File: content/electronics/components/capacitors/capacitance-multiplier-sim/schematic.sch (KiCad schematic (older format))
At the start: 7 parts, among them Q1 2N2222

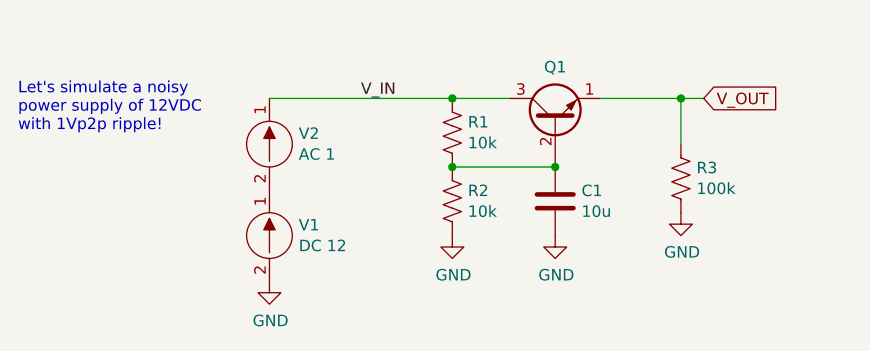
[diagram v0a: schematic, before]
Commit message: Updated the info on capacitance multipliers.
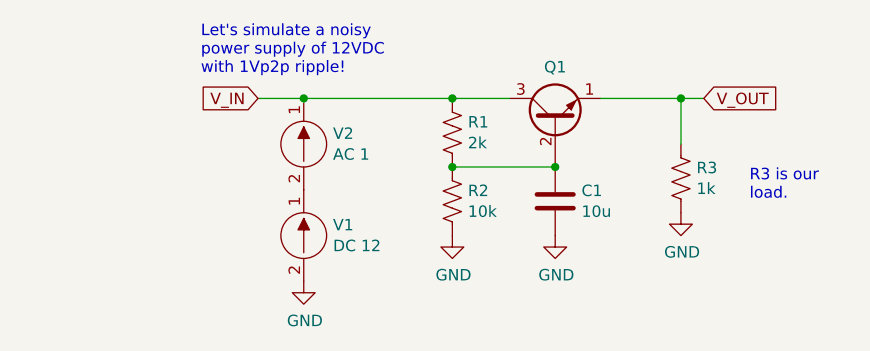
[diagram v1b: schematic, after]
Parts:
- R1: value 10k -> 2k
- R3: value 100k -> 1k
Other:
- note added: "R3 is our\nload."
- moved on the sheet: V1, V2
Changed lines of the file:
@@
 P 4050 3350
 F 0 "R1" H 3982 3304 50  0000 R CNN
-F 1 "10k" H 3982 3395 50  0000 R CNN
+F 1 "2k" H 3982 3395 50  0000 R CNN
 F 2 "" H 4150 2650 50  0001 L CNN
 F 3 "" H 4050 3350 50  0001 L CNN
@@
 L mbedded-ninja-kicad-symbols-sim:DC12 V1
 U 1 1 60CC44AD
-P 3250 3800
-F 0 "V1" H 3378 3846 50  0000 L CNN
-F 1 "DC 12" H 3378 3755 50  0000 L CNN
-F 2 "" H 3250 3800 50  0000 C CNN
-F 3 "" H 3250 3800 50  0000 C CNN
-F 4 "V" H 3500 3550 60  0001 C CNN "Spice_Primitive"
-F 5 "1 2" H 3500 3650 60  0001 C CNN "Spice_Node_Sequence"
-	1    3250 3800
+P 3400 3800
+F 0 "V1" H 3528 3846 50  0000 L CNN
+F 1 "DC 12" H 3528 3755 50  0000 L CNN
+F 2 "" H 3400 3800 50  0000 C CNN
+F 3 "" H 3400 3800 50  0000 C CNN
+F 4 "V" H 3650 3550 60  0001 C CNN "Spice_Primitive"
+F 5 "1 2" H 3650 3650 60  0001 C CNN "Spice_Node_Sequence"
+	1    3400 3800
 	1    0    0    -1
 $EndComp
@@
 L power:GND #PWR01
 U 1 1 60CC56A7
-P 3250 4000
-F 0 "#PWR01" H 3250 3750 50  0001 C CNN
-F 1 "GND" H 3255 3827 50  0000 C CNN
-F 2 "" H 3250 4000 50  0001 C CNN
-F 3 "" H 3250 4000 50  0001 C CNN
-	1    3250 4000
+P 3400 4000
+F 0 "#PWR01" H 3400 3750 50  0001 C CNN
+F 1 "GND" H 3405 3827 50  0000 C CNN
+F 2 "" H 3400 4000 50  0001 C CNN
+F 3 "" H 3400 4000 50  0001 C CNN
+	1    3400 4000
 	1    0    0    -1
 $EndComp
@@
 Connection ~ 4050 3500
 Connection ~ 4500 3500
-Text Label 3650 3200 0    50   ~ 0
-V_IN
 Text GLabel 5150 3200 2    50   Input ~ 0
 V_OUT
@@
 P 5050 3550
 F 0 "R3" H 4982 3504 50  0000 R CNN
-F 1 "100k" H 4982 3595 50  0000 R CNN
+F 1 "1k" H 4982 3595 50  0000 R CNN
 F 2 "" H 5150 2850 50  0001 L CNN
 F 3 "" H 5050 3550 50  0001 L CNN
@@
 L mbedded-ninja-kicad-symbols-sim:DC12 V2
 U 1 1 60CC4008
-P 3250 3400
-F 0 "V2" H 3378 3446 50  0000 L CNN
-F 1 "AC 1" H 3378 3355 50  0000 L CNN
-F 2 "" H 3250 3400 50  0000 C CNN
-F 3 "" H 3250 3400 50  0000 C CNN
-F 4 "V" H 3500 3150 60  0001 C CNN "Spice_Primitive"
-F 5 "1 2" H 3500 3250 60  0001 C CNN "Spice_Node_Sequence"
-	1    3250 3400
+P 3400 3400
+F 0 "V2" H 3528 3446 50  0000 L CNN
+F 1 "AC 1" H 3528 3355 50  0000 L CNN
+F 2 "" H 3400 3400 50  0000 C CNN
+F 3 "" H 3400 3400 50  0000 C CNN
+F 4 "V" H 3650 3150 60  0001 C CNN "Spice_Primitive"
+F 5 "1 2" H 3650 3250 60  0001 C CNN "Spice_Node_Sequence"
+	1    3400 3400
 	1    0    0    -1
 $EndComp
 Wire Wire Line
-	3250 3200 4050 3200
-Text Notes 2150 3350 0    50   ~ 0
+	3400 3200 4050 3200
+Text Notes 2950 3100 0    50   ~ 0
 Let's simulate a noisy \npower supply of 12VDC\nwith 1Vp2p ripple!
+Text GLabel 3200 3200 0    50   Input ~ 0
+V_IN
+Wire Wire Line
+	3200 3200 3400 3200
+Connection ~ 3400 3200
+Text Notes 5350 3650 0    50   ~ 0
+R3 is our\nload.
 $EndSCHEMATC
